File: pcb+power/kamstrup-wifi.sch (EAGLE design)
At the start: 22 parts, among them T1 BT137, T2 BT137

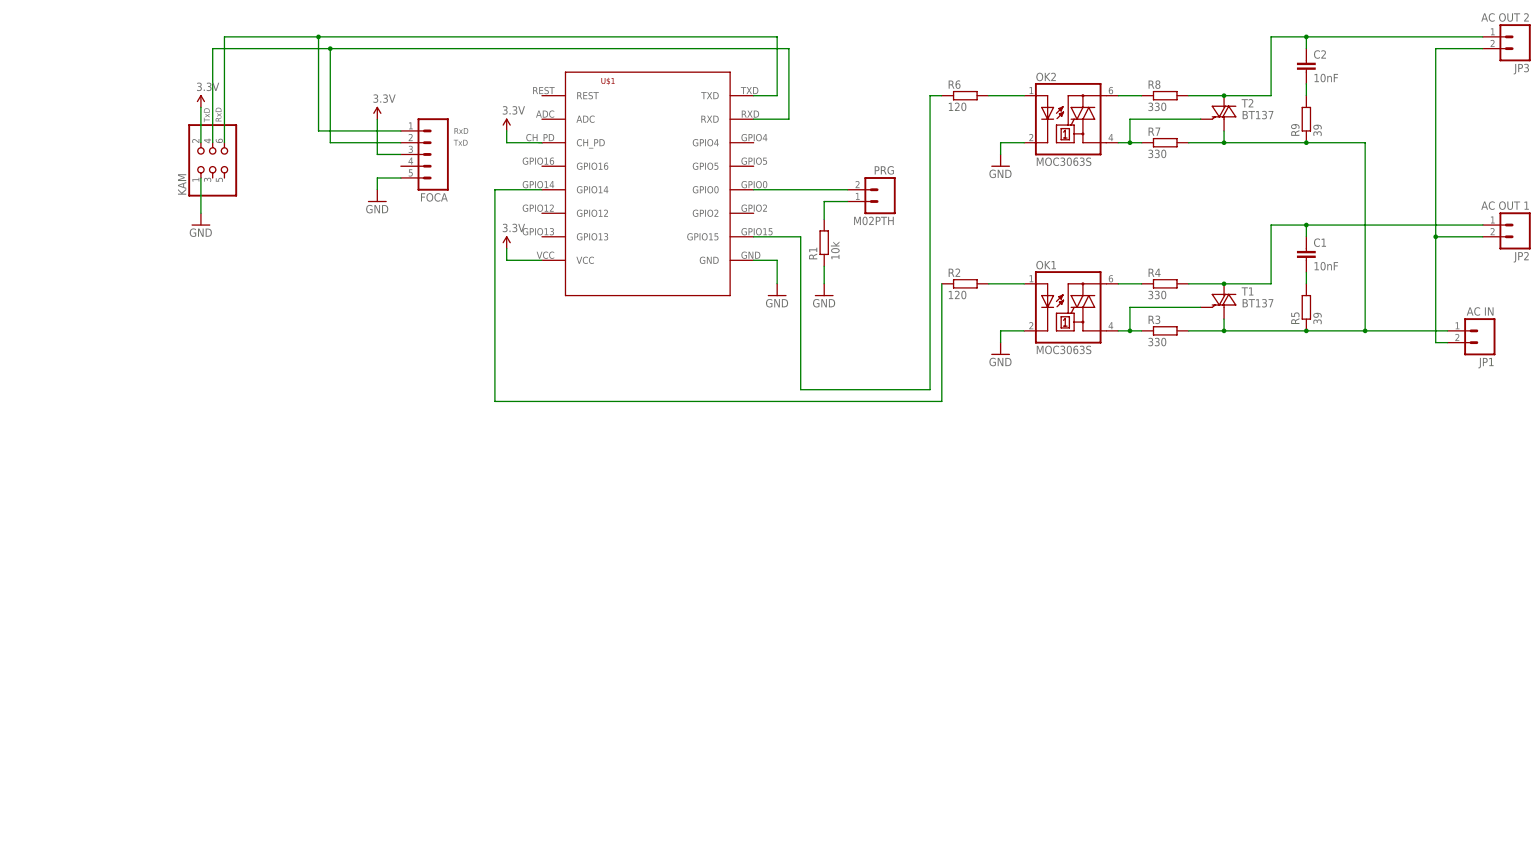
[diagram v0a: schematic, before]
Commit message: v.1.2.1
+ watchdog and pulldown on gpio 15
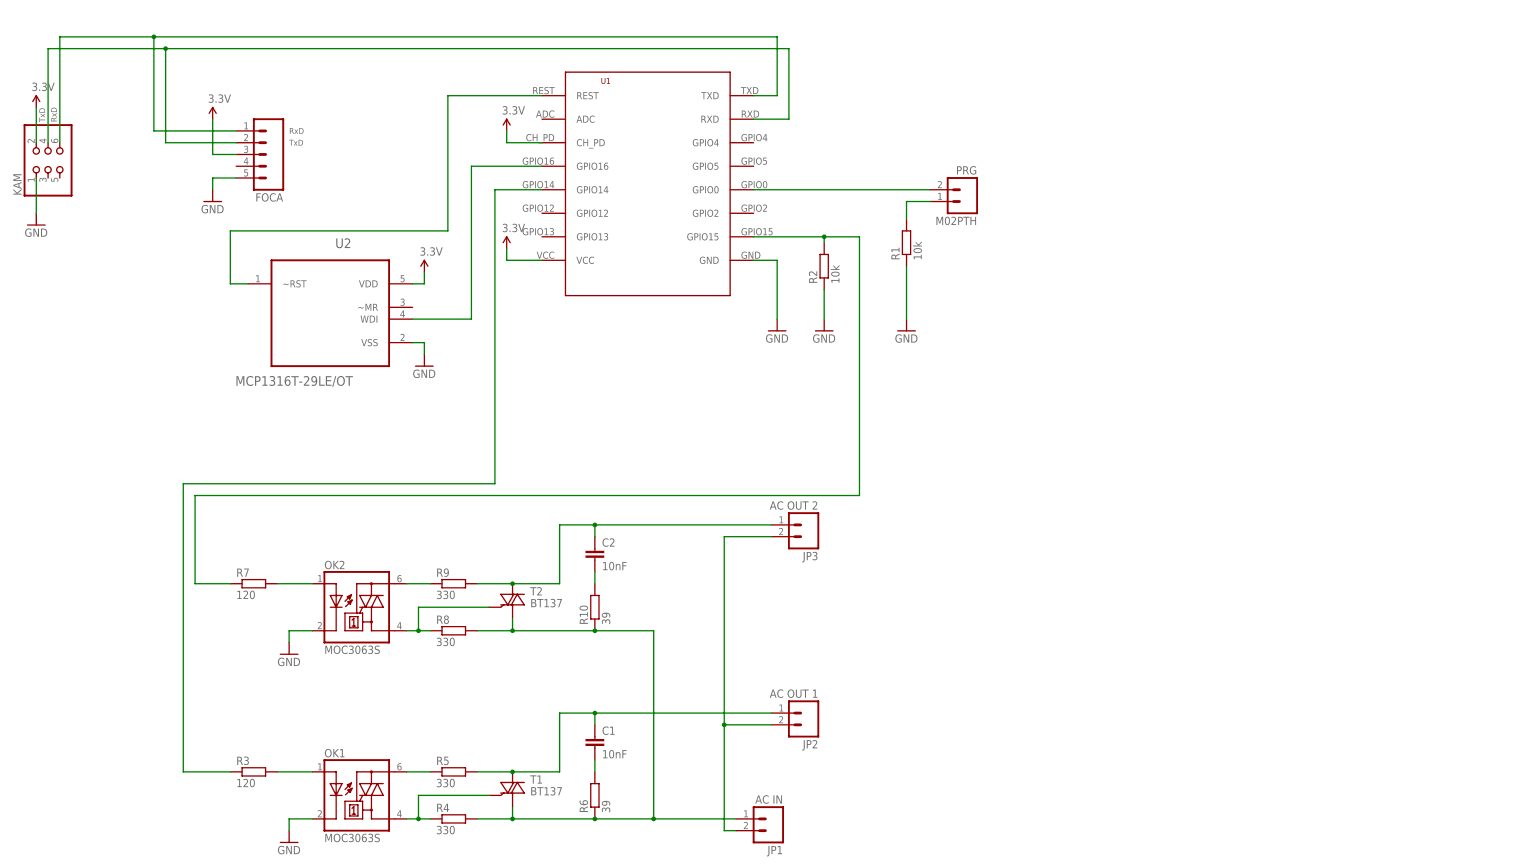
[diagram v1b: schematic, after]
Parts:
- added R10: 39, rcl:R-EU_R0805
- added U2: MCP1316T-29LE/OT, Microchip_By_element14_Batch_1:MCP1316T-29LE/OT
- R2: value 120 -> 10k
- R3, R7: value 330 -> 120
- R5, R9: value 39 -> 330
- R6: value 120 -> 39
- renumbered U$1 to U1
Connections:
- new net N$19: U1.REST, U2.~RST
- new net N$20: U1.GPIO16, U2.WDI
- net 3.3V: now also U2.VDD
- net GND: now also R2.1, U2.VSS
- net N$10: now also R10.2; no longer R9.2
- net N$11: now also R3.1; no longer R2.1
- net N$12: now also R3.2; no longer R2.2
- net N$13: now also R4.1; no longer R3.1
- net N$14: now also R5.1; no longer R4.1
- net N$15: now also R5.2; no longer R4.2
- net N$16: now also R2.2, R7.1; no longer R6.1
- net N$17: now also R6.2; no longer R5.2
- net N$5: now also R7.2; no longer R6.2
- net N$6: now also R8.1; no longer R7.1
- net N$7: now also R9.1; no longer R8.1
- net N$8: now also R9.2; no longer R8.2
- net N$9: now also R10.1, R4.2, R6.1, R8.2; no longer R3.2, R5.1, R7.2, R9.1
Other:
- moved on the sheet: C1, C2, FOCA, JP1, JP2, JP3, KAM, OK1, OK2, PRG, R1, R2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

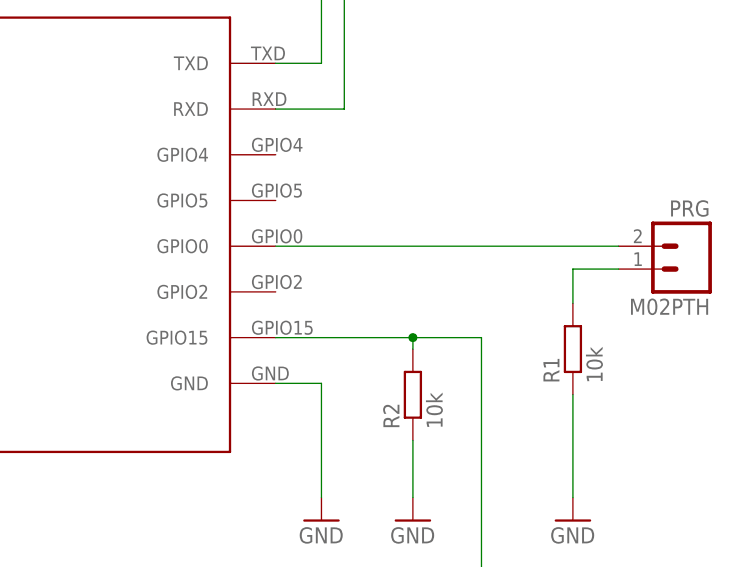
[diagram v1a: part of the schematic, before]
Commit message: added pull up resistor on GPIO02
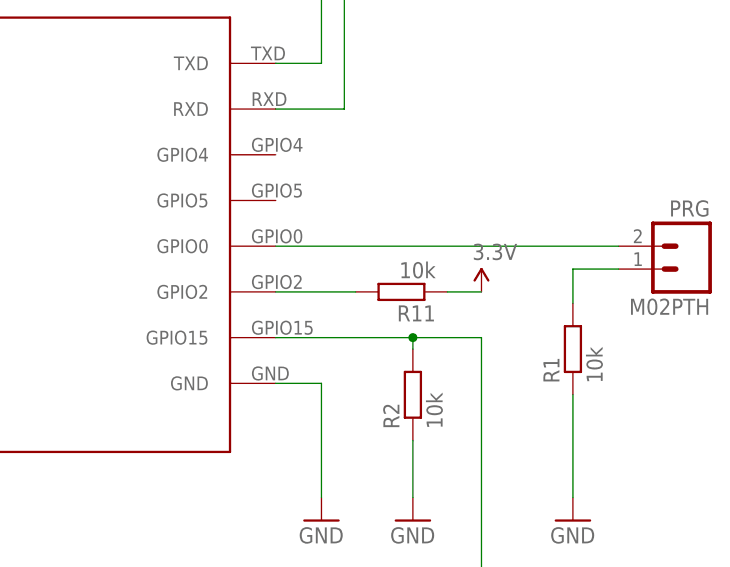
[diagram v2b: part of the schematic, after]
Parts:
- added R11: 10k, rcl:R-EU_R0805
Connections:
- new net N$21: R11.2, U1.GPIO2
- net 3.3V: now also R11.1
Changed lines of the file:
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@@
 <?xml version="1.0" encoding="utf-8"?>
 <!DOCTYPE eagle SYSTEM "eagle.dtd">
-<eagle version="7.2.0">
+<eagle version="7.6.0">
 <drawing>
 <settings>
@@
 <part name="SUPPLY3" library="SparkFun-Aesthetics" deviceset="3.3V" device=""/>
 <part name="GND7" library="SparkFun-Aesthetics" deviceset="GND" device=""/>
+<part name="SUPPLY5" library="SparkFun-Aesthetics" deviceset="3.3V" device=""/>
+<part name="R11" library="rcl" deviceset="R-EU_" device="R0805" value="10k"/>
 </parts>
 <sheets>
@@
 <instance part="SUPPLY3" gate="G$1" x="60.96" y="40.64"/>
 <instance part="GND7" gate="1" x="60.96" y="20.32"/>
+<instance part="SUPPLY5" gate="G$1" x="154.94" y="53.34"/>
+<instance part="R11" gate="G$1" x="146.05" y="53.34" rot="R180"/>
 </instances>
 <busses>
@@
 <wire x1="58.42" y1="38.1" x2="60.96" y2="38.1" width="0.1524" layer="91"/>
 <wire x1="60.96" y1="38.1" x2="60.96" y2="40.64" width="0.1524" layer="91"/>
+</segment>
+<segment>
+<pinref part="R11" gate="G$1" pin="1"/>
+<pinref part="SUPPLY5" gate="G$1" pin="3.3V"/>
+<wire x1="151.13" y1="53.34" x2="154.94" y2="53.34" width="0.1524" layer="91"/>
 </segment>
 </net>
@@
 </segment>
 </net>
+<net name="N$21" class="0">
+<segment>
+<pinref part="R11" gate="G$1" pin="2"/>
+<pinref part="U1" gate="G$1" pin="GPIO2"/>
+<wire x1="140.97" y1="53.34" x2="132.08" y2="53.34" width="0.1524" layer="91"/>
+</segment>
+</net>

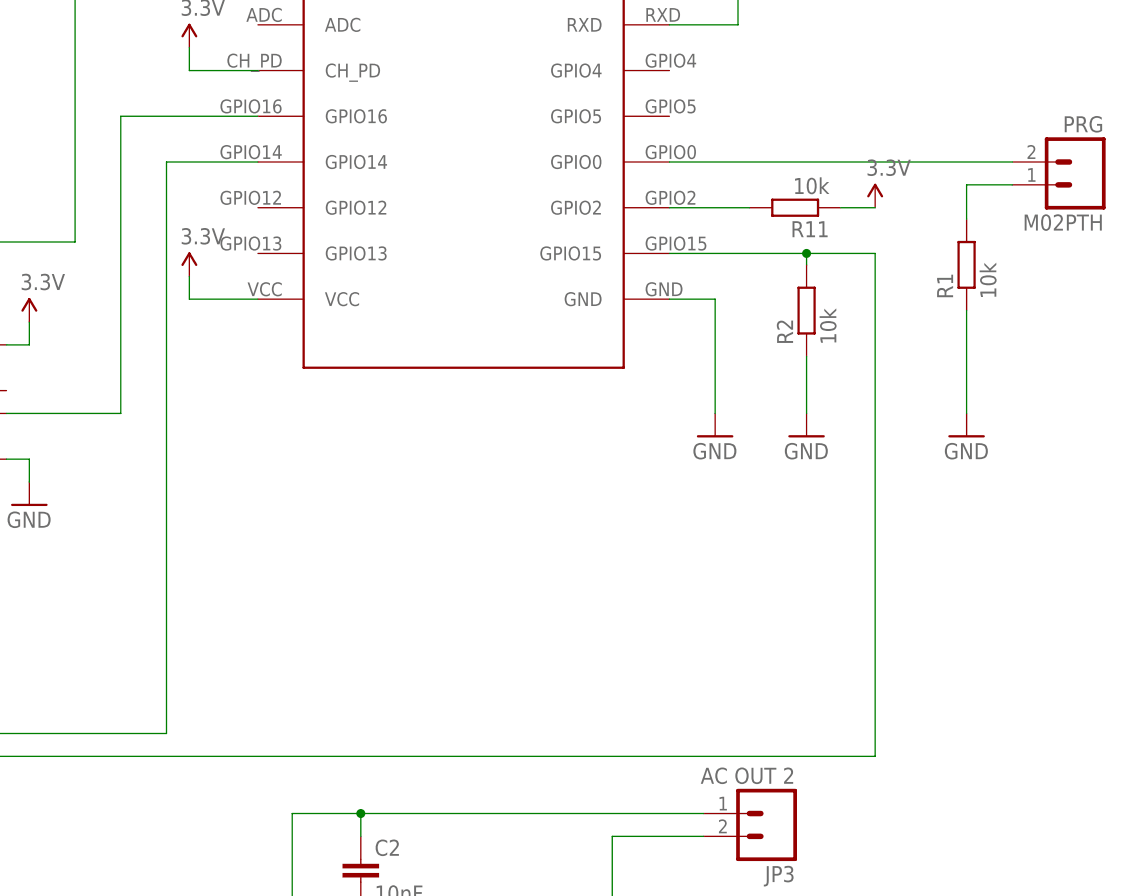
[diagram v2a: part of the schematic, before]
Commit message: added missing pull down (R12) on pcb
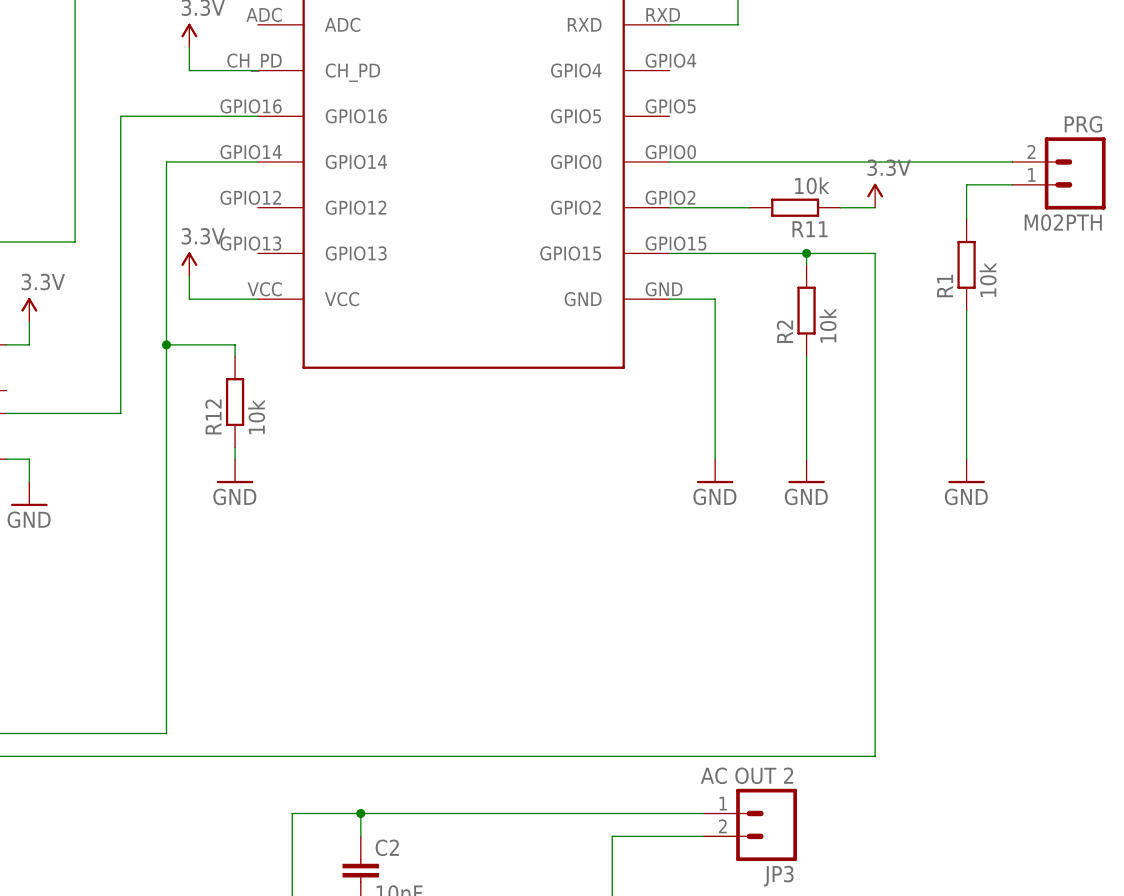
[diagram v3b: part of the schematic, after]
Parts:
- added R12: 10k, rcl:R-EU_R0805
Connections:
- net GND: now also R12.1
- net N$11: now also R12.2
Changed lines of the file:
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@@
 <?xml version="1.0" encoding="utf-8"?>
 <!DOCTYPE eagle SYSTEM "eagle.dtd">
-<eagle version="7.6.0">
+<eagle version="8.1.1">
 <drawing>
 <settings>
@@
 <setting verticaltext="up"/>
 </settings>
-<grid distance="0.05" unitdist="inch" unit="inch" style="lines" multiple="1" display="no" altdistance="0.005" altunitdist="inch" altunit="inch"/>
+<grid distance="0.1" unitdist="inch" unit="inch" style="lines" multiple="1" display="no" altdistance="0.01" altunitdist="inch" altunit="inch"/>
 <layers>
 <layer number="1" name="Top" color="4" fill="1" visible="no" active="no"/>
@@
 <part name="SUPPLY5" library="SparkFun-Aesthetics" deviceset="3.3V" device=""/>
 <part name="R11" library="rcl" deviceset="R-EU_" device="R0805" value="10k"/>
+<part name="R12" library="rcl" deviceset="R-EU_" device="R0805" value="10k"/>
+<part name="GND9" library="SparkFun-Aesthetics" deviceset="GND" device=""/>
 </parts>
 <sheets>
@@
 <attribute name="NAME" x="180.34" y="61.722" size="1.778" layer="95" rot="MR0"/>
 </instance>
-<instance part="GND5" gate="1" x="165.1" y="27.94"/>
+<instance part="GND5" gate="1" x="165.1" y="22.86"/>
 <instance part="R1" gate="G$1" x="165.1" y="46.99" rot="R90"/>
 <instance part="OK2" gate="-1" x="46.99" y="-31.75"/>
@@
 <instance part="T2" gate="G$1" x="80.01" y="-31.75"/>
 <instance part="U1" gate="G$1" x="106.68" y="53.34"/>
-<instance part="GND8" gate="1" x="137.16" y="27.94"/>
+<instance part="GND8" gate="1" x="137.16" y="22.86"/>
 <instance part="SUPPLY2" gate="G$1" x="78.74" y="71.12"/>
 <instance part="SUPPLY7" gate="G$1" x="78.74" y="45.72"/>
 <instance part="U2" gate="A" x="40.64" y="35.56" rot="MR0"/>
 <instance part="R2" gate="G$1" x="147.32" y="41.91" rot="R90"/>
-<instance part="GND3" gate="1" x="147.32" y="27.94"/>
+<instance part="GND3" gate="1" x="147.32" y="22.86"/>
 <instance part="SUPPLY3" gate="G$1" x="60.96" y="40.64"/>
 <instance part="GND7" gate="1" x="60.96" y="20.32"/>
 <instance part="SUPPLY5" gate="G$1" x="154.94" y="53.34"/>
 <instance part="R11" gate="G$1" x="146.05" y="53.34" rot="R180"/>
+<instance part="R12" gate="G$1" x="83.82" y="31.75" rot="R90"/>
+<instance part="GND9" gate="1" x="83.82" y="22.86"/>
 </instances>
 <busses>
@@
 <pinref part="GND5" gate="1" pin="GND"/>
 <pinref part="R1" gate="G$1" pin="1"/>
-<wire x1="165.1" y1="30.48" x2="165.1" y2="41.91" width="0.1524" layer="91"/>
+<wire x1="165.1" y1="25.4" x2="165.1" y2="41.91" width="0.1524" layer="91"/>
 </segment>
 <segment>
@@
 <pinref part="GND8" gate="1" pin="GND"/>
 <wire x1="132.08" y1="43.18" x2="137.16" y2="43.18" width="0.1524" layer="91"/>
-<wire x1="137.16" y1="43.18" x2="137.16" y2="30.48" width="0.1524" layer="91"/>
+<wire x1="137.16" y1="43.18" x2="137.16" y2="25.4" width="0.1524" layer="91"/>
 </segment>
 <segment>
 <pinref part="GND3" gate="1" pin="GND"/>
 <pinref part="R2" gate="G$1" pin="1"/>
-<wire x1="147.32" y1="30.48" x2="147.32" y2="36.83" width="0.1524" layer="91"/>
+<wire x1="147.32" y1="25.4" x2="147.32" y2="36.83" width="0.1524" layer="91"/>
 </segment>
 <segment>
@@
 <wire x1="58.42" y1="25.4" x2="60.96" y2="25.4" width="0.1524" layer="91"/>
 <wire x1="60.96" y1="25.4" x2="60.96" y2="22.86" width="0.1524" layer="91"/>
+</segment>
+<segment>
+<pinref part="GND9" gate="1" pin="GND"/>
+<pinref part="R12" gate="G$1" pin="1"/>
+<wire x1="83.82" y1="25.4" x2="83.82" y2="26.67" width="0.1524" layer="91"/>
 </segment>
 </net>
@@
 <net name="N$11" class="0">
 <segment>
-<wire x1="76.2" y1="-5.08" x2="76.2" y2="58.42" width="0.1524" layer="91"/>
+<wire x1="76.2" y1="-5.08" x2="76.2" y2="38.1" width="0.1524" layer="91"/>
 <pinref part="U1" gate="G$1" pin="GPIO14"/>
+<wire x1="76.2" y1="38.1" x2="76.2" y2="58.42" width="0.1524" layer="91"/>
 <wire x1="76.2" y1="58.42" x2="86.36" y2="58.42" width="0.1524" layer="91"/>
 <wire x1="76.2" y1="-5.08" x2="8.89" y2="-5.08" width="0.1524" layer="91"/>
@@
 <pinref part="R3" gate="G$1" pin="1"/>
 <wire x1="8.89" y1="-67.31" x2="19.05" y2="-67.31" width="0.1524" layer="91"/>
-</segment>
-</net>
+<pinref part="R12" gate="G$1" pin="2"/>
+<wire x1="83.82" y1="36.83" x2="83.82" y2="38.1" width="0.1524" layer="91"/>
+<wire x1="83.82" y1="38.1" x2="76.2" y2="38.1" width="0.1524" layer="91"/>
+<junction x="76.2" y="38.1"/>
+</segment>
+</net>
